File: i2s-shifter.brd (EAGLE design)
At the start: 93.7 x 43.2 mm, 28 parts, among them IC1 74HC164D, IC2 74HC164D, IC3 74HC164D, IC4 74HC164D, IC5 74HC164D

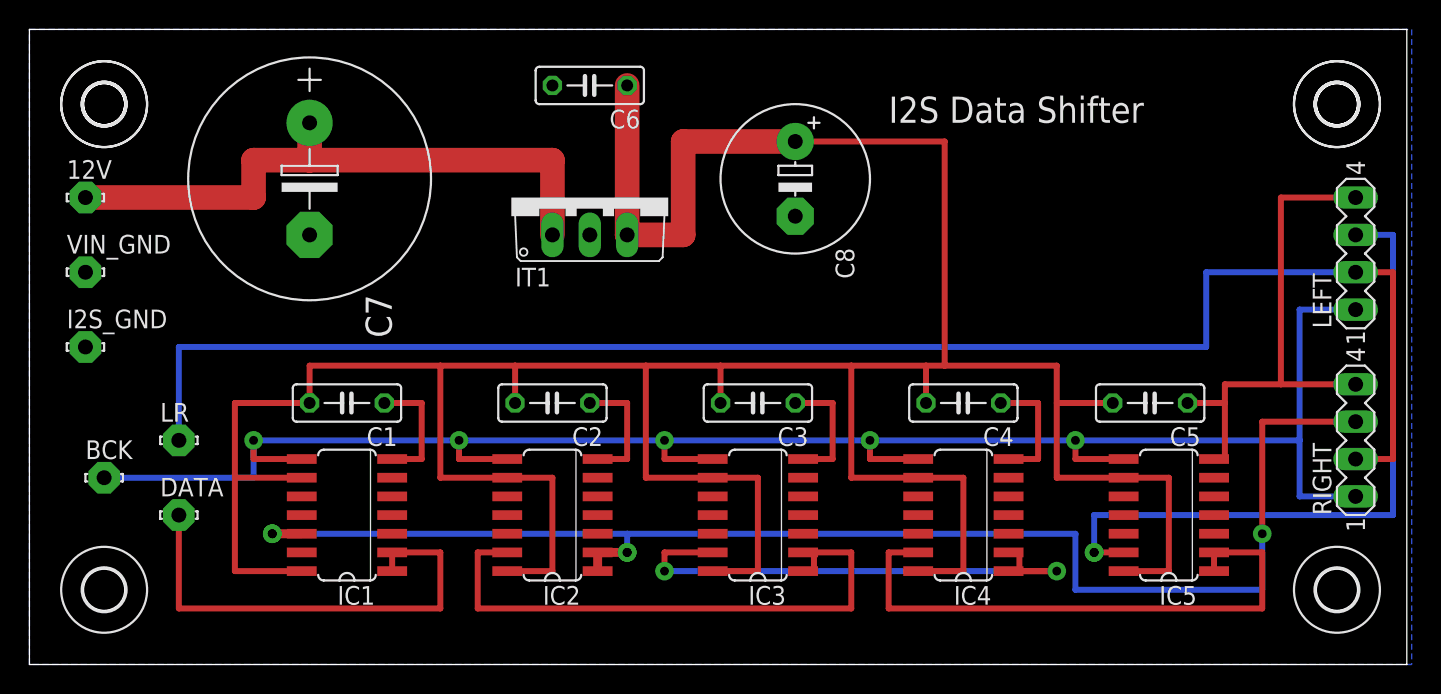
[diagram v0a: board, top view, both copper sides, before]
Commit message: moved caps closer to vcc
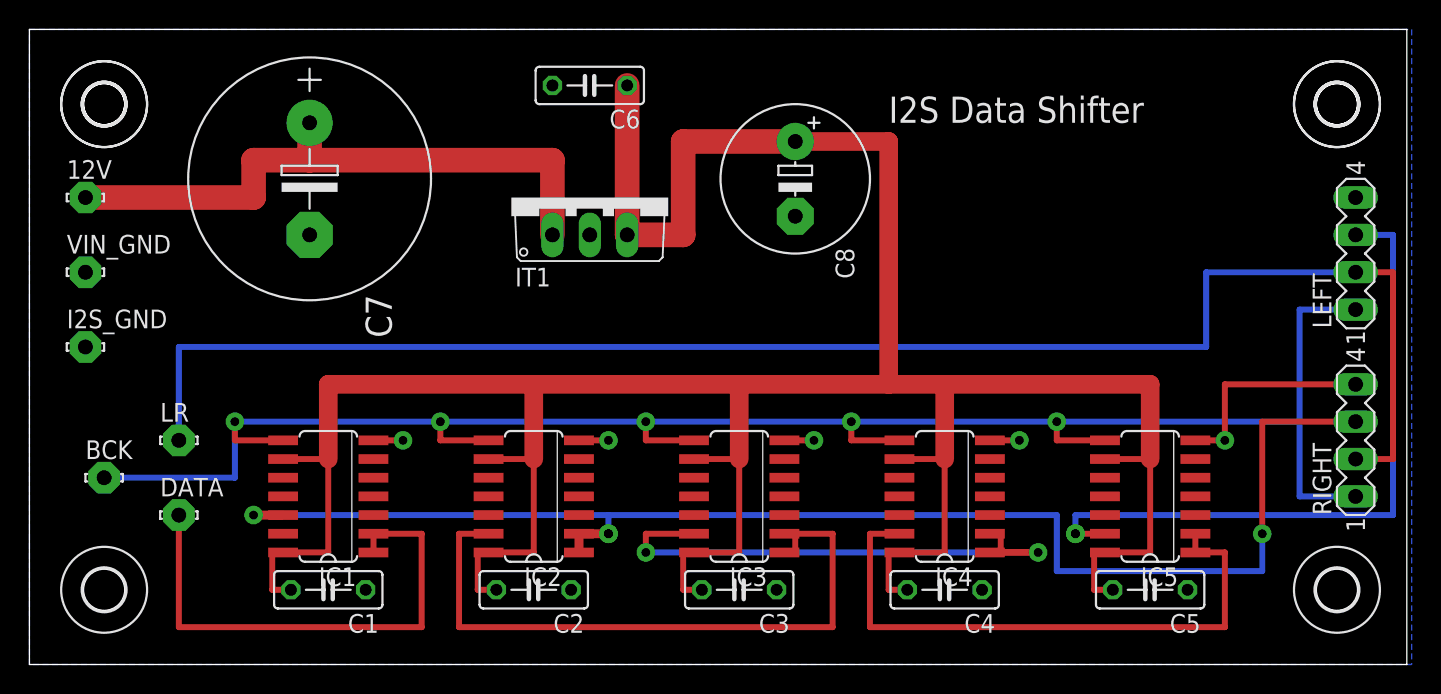
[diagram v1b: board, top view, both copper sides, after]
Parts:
- moved C1 12.8 mm to (20.3, 5.08)
- moved C2 12.8 mm to (34.3, 5.08)
- moved C3 12.8 mm to (48.3, 5.08)
- moved C4 12.8 mm to (62.2, 5.08)
- moved C5 12.7 mm to (76.2, 5.08)
- moved IC2 1.80 mm to (34.3, 11.4)
- moved IC3 1.80 mm to (48.3, 11.4)
- moved IC4 1.80 mm to (62.2, 11.4)
- moved IC1 1.80 mm to (20.3, 11.4)
- moved IC5 1.80 mm to (76.2, 11.4)
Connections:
- net GND renamed NS999
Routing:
- net NS999: track 68.5 -> 22.7 mm, vias 0 -> 5
- net +3V3: track 242.4 -> 217.3 mm
- net N$4: track 40.3 -> 45.4 mm
- net N$1: track 32.5 -> 35.0 mm
- net N$6: track 39.6 -> 40.8 mm
- net N$2: track 127.4 -> 128.7 mm
